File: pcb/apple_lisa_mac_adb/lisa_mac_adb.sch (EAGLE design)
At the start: 54 parts, among them IC1 STM32F072C8T6, SW1 324_SW, SW2 324_SW, SW3 324_SW

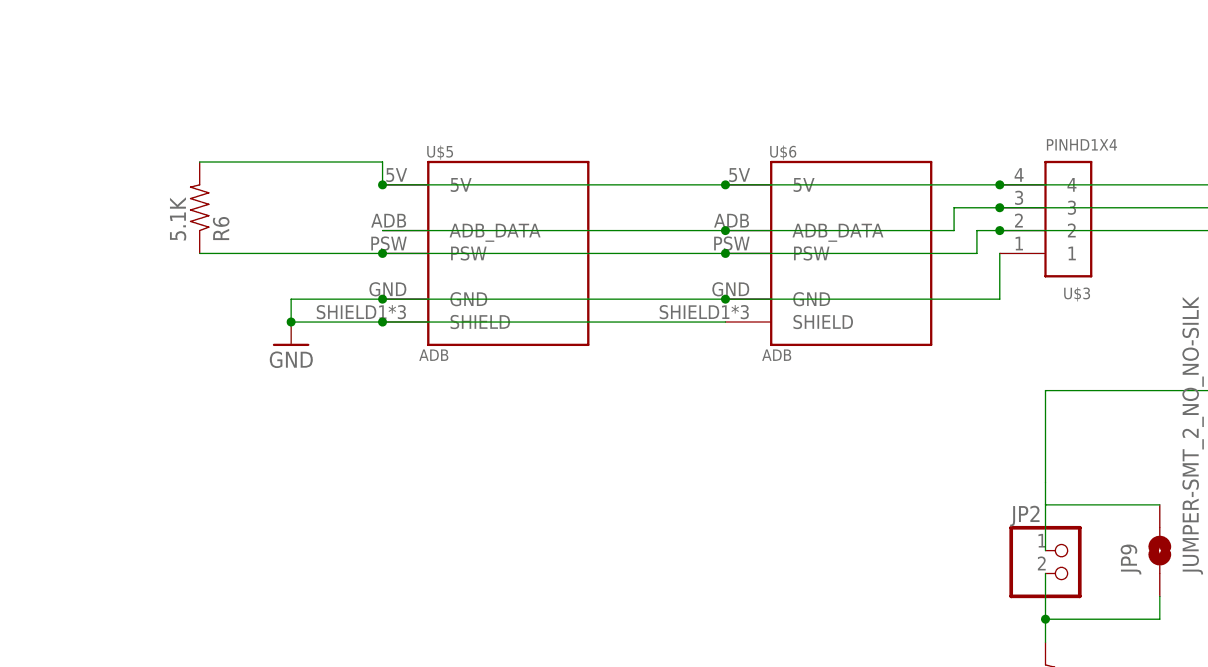
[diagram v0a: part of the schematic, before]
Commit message: removed ADB power button pullup resistor
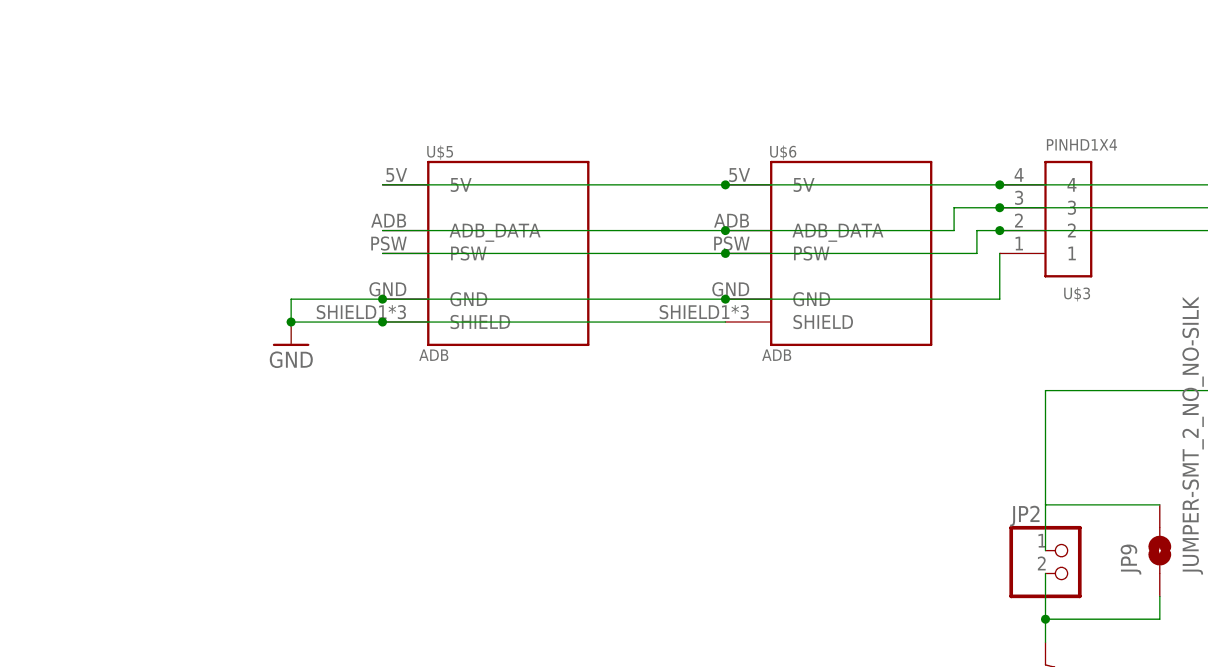
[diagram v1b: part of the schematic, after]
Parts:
- removed R6: 5.1K, SparkFun-Passives:RESISTOR0805-RES
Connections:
- net N$3: no longer R6.2
- net N$46: no longer R6.1
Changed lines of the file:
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@@
 <?xml version="1.0" encoding="utf-8"?>
 <!DOCTYPE eagle SYSTEM "eagle.dtd">
-<eagle version="9.6.1">
+<eagle version="9.6.2">
 <drawing>
 <settings>
@@
 <part name="GND19" library="supply1" library_urn="urn:adsk.eagle:library:371" deviceset="GND" device=""/>
 <part name="JP2" library="pinhead" library_urn="urn:adsk.eagle:library:325" deviceset="PINHD-1X2" device="" package3d_urn="urn:adsk.eagle:package:22435/2"/>
-<part name="R6" library="SparkFun-Passives" deviceset="RESISTOR" device="0805-RES" value="5.1K"/>
 <part name="R17" library="SparkFun-Passives" deviceset="RESISTOR" device="0805-RES" value="100"/>
 <part name="TP2" library="testpad" library_urn="urn:adsk.eagle:library:385" deviceset="PTR1" device="TP14R" package3d_urn="urn:adsk.eagle:package:27966/1"/>
@@
 <attribute name="VALUE" x="62.23" y="86.36" size="1.778" layer="96"/>
 </instance>
-<instance part="R6" gate="G$1" x="-27.94" y="132.08" smashed="yes" rot="MR90">
-<attribute name="NAME" x="-26.4414" y="128.27" size="1.778" layer="95" rot="MR90"/>
-<attribute name="VALUE" x="-31.242" y="128.27" size="1.778" layer="96" rot="MR90"/>
-</instance>
 <instance part="R17" gate="G$1" x="342.9" y="12.7" smashed="yes">
 <attribute name="NAME" x="339.09" y="14.1986" size="1.778" layer="95"/>
@@
 <junction x="60.96" y="134.62"/>
 <wire x1="91.44" y1="134.62" x2="91.44" y2="180.34" width="0.1524" layer="91"/>
-<pinref part="R6" gate="G$1" pin="2"/>
-<wire x1="-7.62" y1="134.62" x2="-7.62" y2="137.16" width="0.1524" layer="91"/>
-<wire x1="-7.62" y1="137.16" x2="-27.94" y2="137.16" width="0.1524" layer="91"/>
-<junction x="-7.62" y="134.62"/>
 <wire x1="91.44" y1="180.34" x2="73.66" y2="180.34" width="0.1524" layer="91"/>
 <pinref part="R10" gate="G$1" pin="2"/>
@@
 <wire x1="66.04" y1="93.98" x2="66.04" y2="99.06" width="0.1524" layer="91"/>
 <pinref part="JP2" gate="G$1" pin="1"/>
-<pinref part="R6" gate="G$1" pin="1"/>
-<wire x1="66.04" y1="101.6" x2="66.04" y2="111.76" width="0.1524" layer="91"/>
-<wire x1="-7.62" y1="127" x2="-27.94" y2="127" width="0.1524" layer="91"/>
-<junction x="-7.62" y="127"/>
+<wire x1="66.04" y1="99.06" x2="66.04" y2="111.76" width="0.1524" layer="91"/>
 <pinref part="JP9" gate="G$1" pin="2"/>
 <wire x1="78.74" y1="99.06" x2="66.04" y2="99.06" width="0.1524" layer="91"/>
-<wire x1="66.04" y1="99.06" x2="66.04" y2="101.6" width="0.1524" layer="91"/>
-</segment>
-</net>
+</segment>
+</net>
